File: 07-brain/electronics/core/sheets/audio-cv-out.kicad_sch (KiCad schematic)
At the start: 26 parts, among them U4 TL072, U5 TL072, U6 MCP4822, U7 74HC4053B

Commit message: Design Brain/Core PCB
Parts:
- U4, U5: footprint (none) -> Package_SO:SOIC-8_3.9x4.9mm_P1.27mm
- U6: footprint Package_DIP:DIP-8_W7.62mm_LongPads -> Package_SO:SOIC-8_3.9x4.9mm_P1.27mm
- U7: footprint (none) -> Package_SO:SOIC-16_3.9x9.9mm_P1.27mm
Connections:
- net GND is gone; now on net GNDA: R16.1, R17.1, U7.12 (A0), U7.2 (B0)
- net at R14.2, R16.2: now also U4.5 (+); no longer U4.6 (-)
- net at R19.1, R20.1: now also U4.6 (-); no longer U4.5 (+)
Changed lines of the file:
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@@
 	)
 	(junction
+		(at 116.84 110.49)
+		(diameter 0)
+		(color 0 0 0 0)
+	)
+	(junction
 		(at 179.07 137.16)
 		(diameter 0)
@@
 	(wire
 		(pts
+			(xy 106.68 110.49) (xy 116.84 110.49)
+		)
+		(stroke
+			(width 0)
+			(type default)
+		)
+	)
+	(wire
+		(pts
 			(xy 158.75 137.16) (xy 166.37 137.16)
 		)
@@
 	(wire
 		(pts
-			(xy 106.68 92.71) (xy 106.68 101.6)
+			(xy 106.68 92.71) (xy 106.68 110.49)
 		)
 		(stroke
@@
 			)
 		)
-		(property "Footprint" ""
+		(property "Footprint" "Package_SO:SOIC-8_3.9x4.9mm_P1.27mm"
 			(at 213.36 33.02 0)
 			(effects
@@
 		(lib_id "Amplifier_Operational:TL072")
 		(at 212.09 134.62 0)
+		(mirror x)
 		(unit 2)
 		(exclude_from_sim no)
@@
 		(dnp no)
 		(property "Reference" "U4"
-			(at 214.63 139.7 0)
+			(at 214.63 129.54 0)
 			(effects
 				(font
@@
 		)
 		(property "Value" "TL072"
-			(at 214.63 142.24 0)
+			(at 214.63 127 0)
 			(effects
 				(font
@@
 			)
 		)
-		(property "Footprint" ""
+		(property "Footprint" "Package_SO:SOIC-8_3.9x4.9mm_P1.27mm"
 			(at 212.09 134.62 0)
 			(effects
@@
 			)
 		)
-		(property "Footprint" ""
+		(property "Footprint" "Package_SO:SOIC-8_3.9x4.9mm_P1.27mm"
 			(at 41.91 176.53 0)
 			(effects
@@
 			)
 		)
-		(property "Footprint" "Package_DIP:DIP-8_W7.62mm_LongPads"
+		(property "Footprint" "Package_SO:SOIC-8_3.9x4.9mm_P1.27mm"
 			(at 77.47 93.98 0)
 			(effects
@@
 			)
 		)
-		(property "Footprint" ""
+		(property "Footprint" "Package_SO:SOIC-8_3.9x4.9mm_P1.27mm"
 			(at 133.35 30.48 0)
 			(effects
@@
 	)
 	(symbol
-		(lib_id "power:GND")
-		(at 106.68 101.6 0)
-		(unit 1)
-		(exclude_from_sim no)
-		(in_bom yes)
-		(on_board yes)
-		(dnp no)
-		(fields_autoplaced yes)
-		(property "Reference" "#PWR044"
-			(at 106.68 107.95 0)
-			(effects
-				(font
-					(size 1.27 1.27)
-				)
-				(hide yes)
-			)
-		)
-		(property "Value" "GND"
-			(at 106.68 106.68 0)
-			(effects
-				(font
-					(size 1.27 1.27)
-				)
-			)
-		)
-		(property "Footprint" ""
-			(at 106.68 101.6 0)
-			(effects
-				(font
-					(size 1.27 1.27)
-				)
-				(hide yes)
-			)
-		)
-		(property "Datasheet" ""
-			(at 106.68 101.6 0)
-			(effects
-				(font
-					(size 1.27 1.27)
-				)
-				(hide yes)
-			)
-		)
-		(property "Description" "Power symbol creates a global label with name \"GND\" , ground"
-			(at 106.68 101.6 0)
-			(effects
-				(font
-					(size 1.27 1.27)
-				)
-				(hide yes)
-			)
-		)
-		(pin "1"
-		)
-		(instances
-			(project ""
-				(path "/8e2e31f3-eed5-4de1-966c-f4162758c735/a5dac03c-0548-4574-b19b-4dd5fbd38e47"
-					(reference "#PWR044")
-					(unit 1)
-				)
-			)
-		)
-	)
-	(symbol
 		(lib_id "Device:R")
 		(at 151.13 137.16 90)
@@
 	(symbol
 		(lib_id "power:GNDA")
+		(at 180.34 44.45 0)
+		(unit 1)
+		(exclude_from_sim no)
+		(in_bom yes)
+		(on_board yes)
+		(dnp no)
+		(fields_autoplaced yes)
+		(property "Reference" "#PWR051"
+			(at 180.34 50.8 0)
+			(effects
+				(font
+					(size 1.27 1.27)
+				)
+				(hide yes)
+			)
+		)
+		(property "Value" "GNDA"
+			(at 180.34 49.53 0)
+			(effects
+				(font
+					(size 1.27 1.27)
+				)
+			)
+		)
+		(property "Footprint" ""
+			(at 180.34 44.45 0)
+			(effects
+				(font
+					(size 1.27 1.27)
+				)
+				(hide yes)
+			)
+		)
+		(property "Datasheet" ""
+			(at 180.34 44.45 0)
+			(effects
+				(font
+					(size 1.27 1.27)
+				)
+				(hide yes)
+			)
+		)
+		(property "Description" "Power symbol creates a global label with name \"GNDA\" , analog ground"
+			(at 180.34 44.45 0)
+			(effects
+				(font
+					(size 1.27 1.27)
+				)
+				(hide yes)
+			)
+		)
+		(pin "1"
+		)
+		(instances
+			(project "brain-core"
+				(path "/8e2e31f3-eed5-4de1-966c-f4162758c735/a5dac03c-0548-4574-b19b-4dd5fbd38e47"
+					(reference "#PWR051")
+					(unit 1)
+				)
+			)
+		)
+	)
+	(symbol
+		(lib_id "power:GNDA")
 		(at 41.91 101.6 0)
 		(unit 1)
@@
 	)
 	(symbol
+		(lib_id "power:GNDA")
+		(at 179.07 151.13 0)
+		(unit 1)
+		(exclude_from_sim no)
+		(in_bom yes)
+		(on_board yes)
+		(dnp no)
+		(fields_autoplaced yes)
+		(property "Reference" "#PWR050"
+			(at 179.07 157.48 0)
+			(effects
+				(font
+					(size 1.27 1.27)
+				)
+				(hide yes)
+			)
+		)
+		(property "Value" "GNDA"
+			(at 179.07 156.21 0)
+			(effects
+				(font
+					(size 1.27 1.27)
+				)
+			)
+		)
+		(property "Footprint" ""
+			(at 179.07 151.13 0)
+			(effects
+				(font
+					(size 1.27 1.27)
+				)
+				(hide yes)
+			)
+		)
+		(property "Datasheet" ""
+			(at 179.07 151.13 0)
+			(effects
+				(font
+					(size 1.27 1.27)
+				)
+				(hide yes)
+			)
+		)
+		(property "Description" "Power symbol creates a global label with name \"GNDA\" , analog ground"
+			(at 179.07 151.13 0)
+			(effects
+				(font
+					(size 1.27 1.27)
+				)
+				(hide yes)
+			)
+		)
+		(pin "1"
+		)
+		(instances
+			(project "brain-core"
+				(path "/8e2e31f3-eed5-4de1-966c-f4162758c735/a5dac03c-0548-4574-b19b-4dd5fbd38e47"
+					(reference "#PWR050")
+					(unit 1)
+				)
+			)
+		)
+	)
+	(symbol
 		(lib_id "Device:C")
 		(at 133.35 39.37 90)
@@
 			)
 		)
-		(property "Footprint" ""
+		(property "Footprint" "Package_SO:SOIC-8_3.9x4.9mm_P1.27mm"
 			(at 24.13 176.53 0)
 			(effects
@@
 	)
 	(symbol
-		(lib_id "power:GND")
-		(at 180.34 44.45 0)
-		(unit 1)
-		(exclude_from_sim no)
-		(in_bom yes)
-		(on_board yes)
-		(dnp no)
-		(fields_autoplaced yes)
-		(property "Reference" "#PWR051"
-			(at 180.34 50.8 0)
-			(effects
-				(font
-					(size 1.27 1.27)
-				)
-				(hide yes)
-			)
-		)
-		(property "Value" "GND"
-			(at 180.34 49.53 0)
-			(effects
-				(font
-					(size 1.27 1.27)
-				)
-			)
-		)
-		(property "Footprint" ""
-			(at 180.34 44.45 0)
-			(effects
-				(font
-					(size 1.27 1.27)
-				)
-				(hide yes)
-			)
-		)
-		(property "Datasheet" ""
-			(at 180.34 44.45 0)
-			(effects
-				(font
-					(size 1.27 1.27)
-				)
-				(hide yes)
-			)
-		)
-		(property "Description" "Power symbol creates a global label with name \"GND\" , ground"
-			(at 180.34 44.45 0)
-			(effects
-				(font
-					(size 1.27 1.27)
-				)
-				(hide yes)
-			)
-		)
-		(pin "1"
-		)
-		(instances
-			(project ""
-				(path "/8e2e31f3-eed5-4de1-966c-f4162758c735/a5dac03c-0548-4574-b19b-4dd5fbd38e47"
-					(reference "#PWR051")
-					(unit 1)
-				)
-			)
-		)
-	)
-	(symbol
 		(lib_id "Amplifier_Operational:TL072")
 		(at 132.08 137.16 0)
@@
 			)
 		)
-		(property "Footprint" ""
+		(property "Footprint" "Package_SO:SOIC-8_3.9x4.9mm_P1.27mm"
 			(at 132.08 137.16 0)
 			(effects
@@
 			)
 		)
-		(property "Footprint" ""
+		(property "Footprint" "Package_SO:SOIC-16_3.9x9.9mm_P1.27mm"
 			(at 129.54 109.22 0)
 			(effects
@@
 					(unit 1)
 				)
-			)
-		)
-	)
-	(symbol
-		(lib_id "power:GND")
-		(at 179.07 151.13 0)
-		(unit 1)
-		(exclude_from_sim no)
-		(in_bom yes)
-		(on_board yes)
-		(dnp no)
-		(fields_autoplaced yes)
-		(property "Reference" "#PWR050"
-			(at 179.07 157.48 0)
-			(effects
-				(font
-					(size 1.27 1.27)
-				)
-				(hide yes)
-			)
-		)
-		(property "Value" "GND"
-			(at 179.07 156.21 0)
-			(effects
-				(font
-					(size 1.27 1.27)
-				)
-			)
-		)
-		(property "Footprint" ""
-			(at 179.07 151.13 0)
-			(effects
-				(font
-					(size 1.27 1.27)
-				)
-				(hide yes)
-			)
-		)
-		(property "Datasheet" ""
-			(at 179.07 151.13 0)
-			(effects
-				(font
-					(size 1.27 1.27)
-				)
-				(hide yes)
-			)
-		)
-		(property "Description" "Power symbol creates a global label with name \"GND\" , ground"
-			(at 179.07 151.13 0)
-			(effects
-				(font
-					(size 1.27 1.27)
-				)
-				(hide yes)
-			)
-		)
-		(pin "1"
-		)
-		(instances
-			(project "brain-core"
-				(path "/8e2e31f3-eed5-4de1-966c-f4162758c735/a5dac03c-0548-4574-b19b-4dd5fbd38e47"
-					(reference "#PWR050")
-					(unit 1)
-				)

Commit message: Brain PCB WIP
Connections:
- net GNDA renamed GND

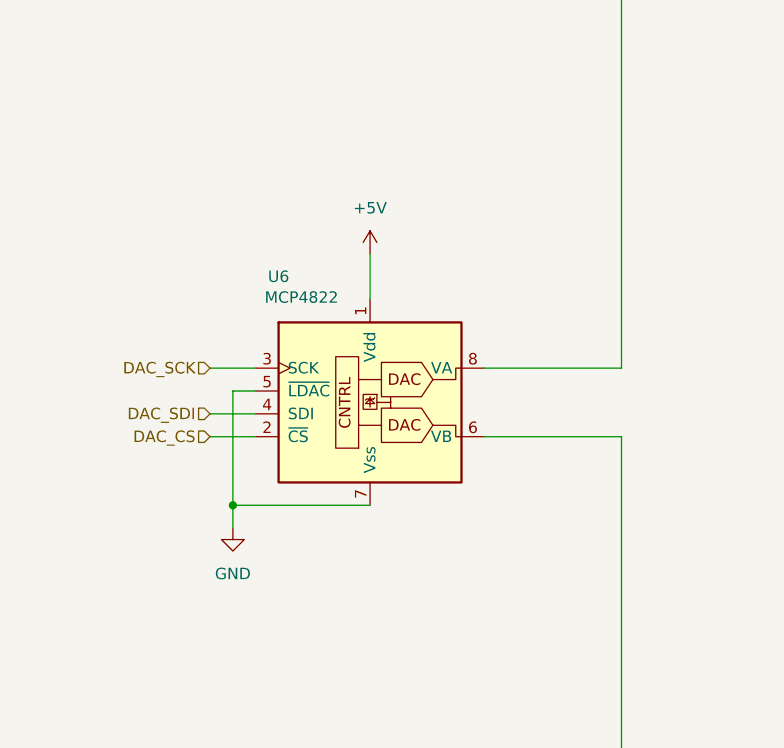
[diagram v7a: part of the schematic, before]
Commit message: Added decoupling caps to DAC in Brain
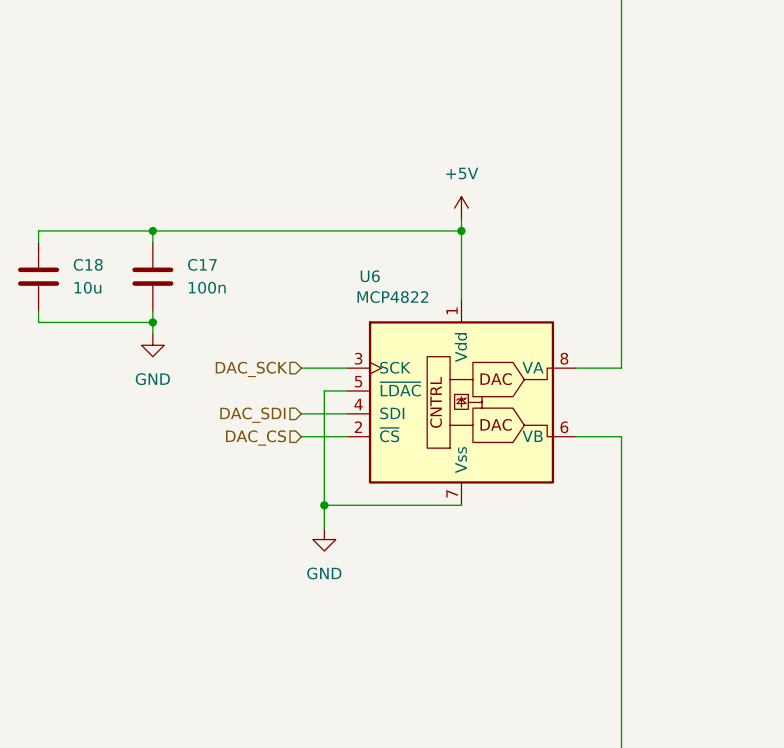
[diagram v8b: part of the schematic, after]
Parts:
- added C17: 100n, Capacitor_SMD:C_0603_1608Metric, symbol Device:C
- added C18: 10u, Capacitor_SMD:C_0603_1608Metric, symbol Device:C
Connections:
- net +5V: now also C17.1, C18.1
- net GND: now also C17.2, C18.2
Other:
- moved on the sheet: U6
